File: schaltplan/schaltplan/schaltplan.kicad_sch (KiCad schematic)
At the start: 26 parts, among them SW1 Button 1, SW2 Button 2, SW3 Button 3, SW4 Button 4

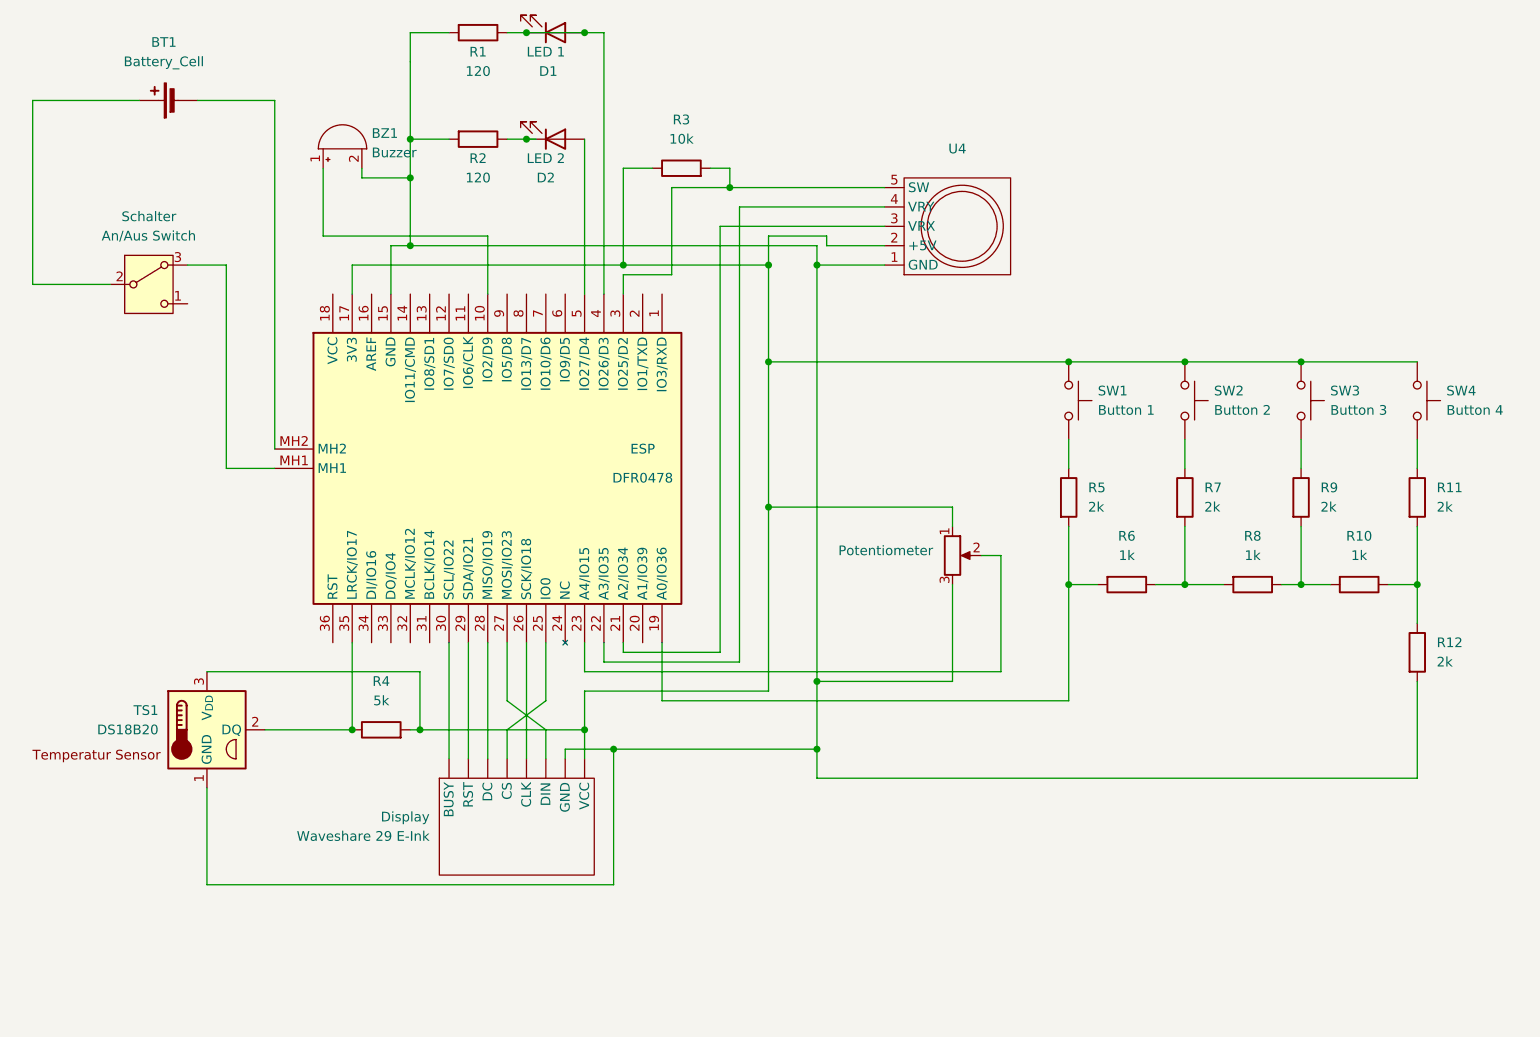
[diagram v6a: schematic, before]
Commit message: schaltplan mit fabians version gemerged
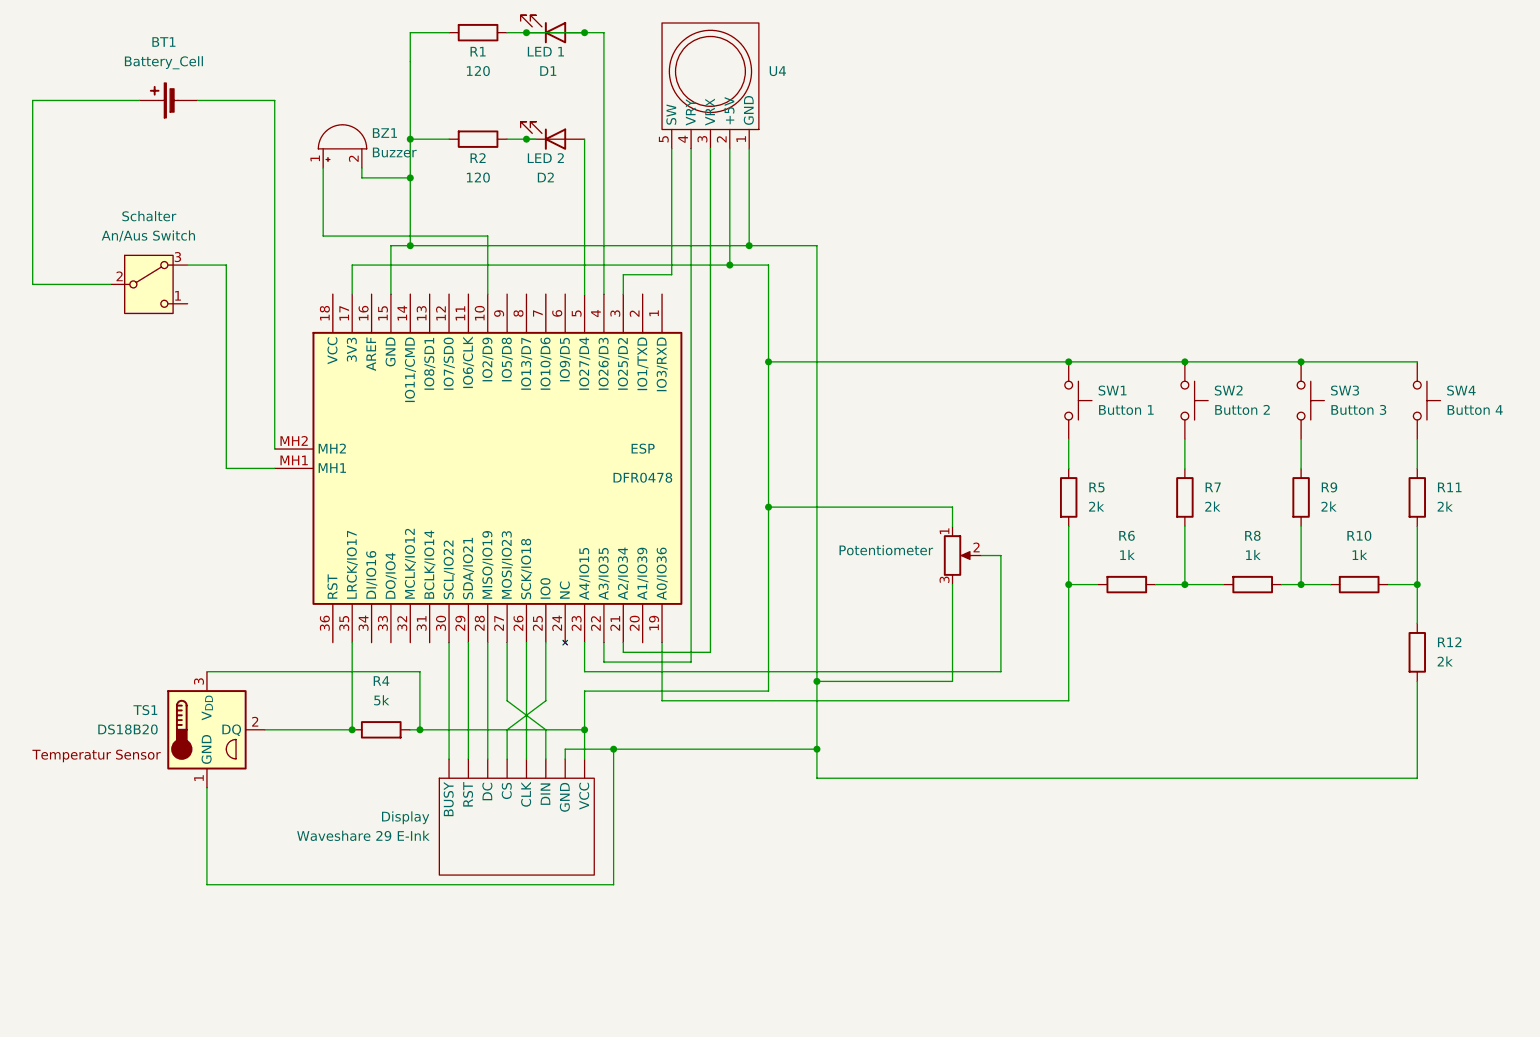
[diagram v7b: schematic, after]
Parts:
- removed R3: 10k, symbol Device:R
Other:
- moved on the sheet: U4

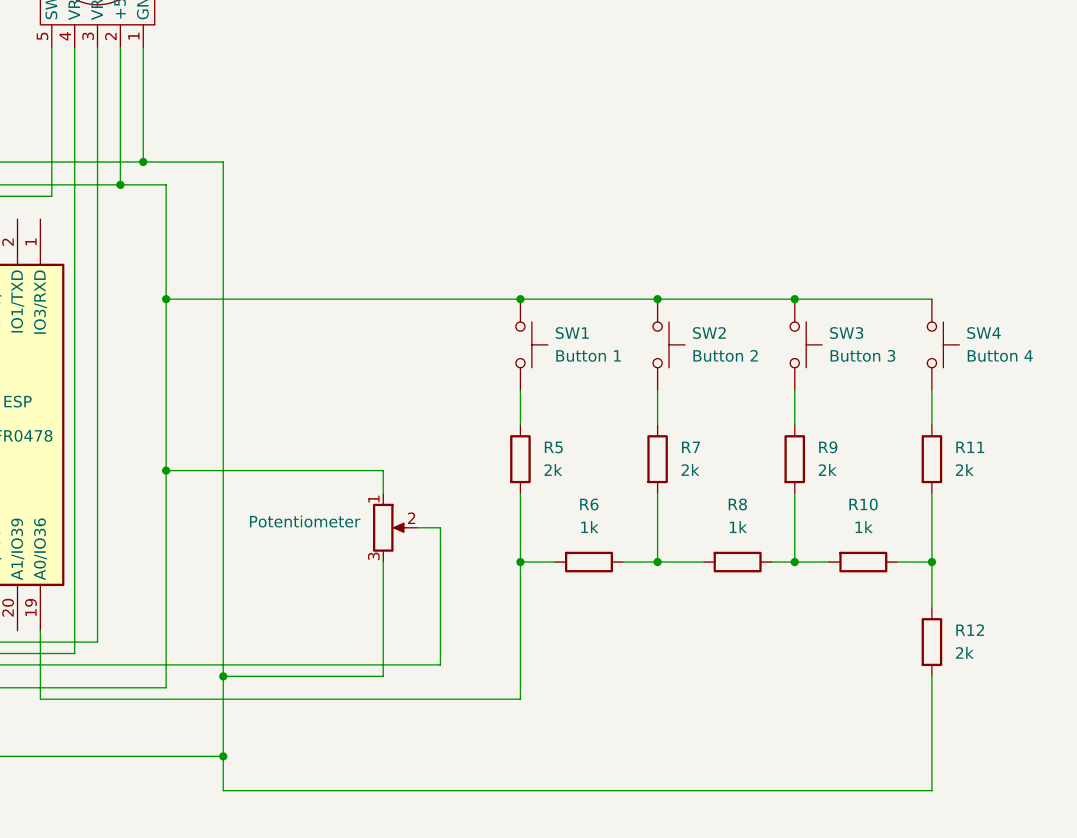
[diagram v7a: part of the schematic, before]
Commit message: digitial analog wandler problem gelöst. das funktionier einigermaßen zuverlässig. schaltplat ergänzt sowie komponente dafür geschrieben. die werte sind jedoch sicherlich sehr individuell :| evtl. sollten wir doch eine i2c pin erweiterung verwenden (falls nötig, denn aktuell haben wir ja eigentlich noch genug pins)
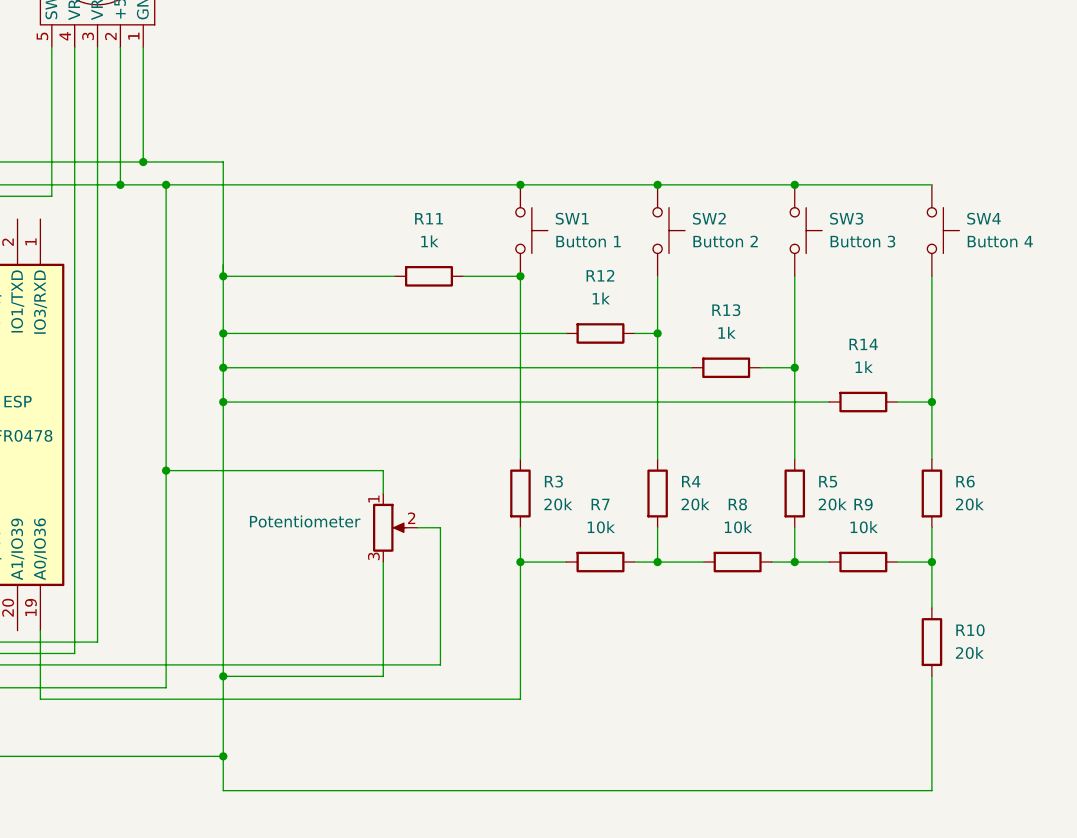
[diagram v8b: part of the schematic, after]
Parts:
- added R11, R12, R13, R14: 1k, symbol Device:R
- R10: renamed from R12; value 2k -> 20k
- R3: renamed from R5; value 2k -> 20k
- R4: renamed from R7; value 2k -> 20k
- R5: renamed from R9; value 2k -> 20k
- R6: renamed from R11; value 2k -> 20k
- R7: renamed from R6; value 1k -> 10k
- R8: value 1k -> 10k
- R9: renamed from R10; value 1k -> 10k
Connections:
- net at BZ1.2 (-), Display. (VCC), ESP.15 (GND)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: now also R11.2, R12.2, R13.2, R14.2
- net at R5.1, SW3.2: now also R13.1
- net at R4.1, SW2.2: now also R12.1
- net at R3.1, SW1.2: now also R11.1
- net at R6.1, SW4.2: now also R14.1
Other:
- moved on the sheet: R3, R4, R5, R6, R7, SW1, SW2, SW3, SW4
